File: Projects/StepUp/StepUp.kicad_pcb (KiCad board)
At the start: 2 copper layers, 53 parts, among them J1 Conn_01x02, J2 USB_B_Micro, U1 TMC2300-LA, U2 NCP1117-3.3_SOT223, U3 MIC2253, U4 W25Q128JVS, U5 RP2040, U6 COM-09032, U7 MCP73832T-2ACI_OT, U8 USBLC6-2SC6, Y1 ABM8-272-T3

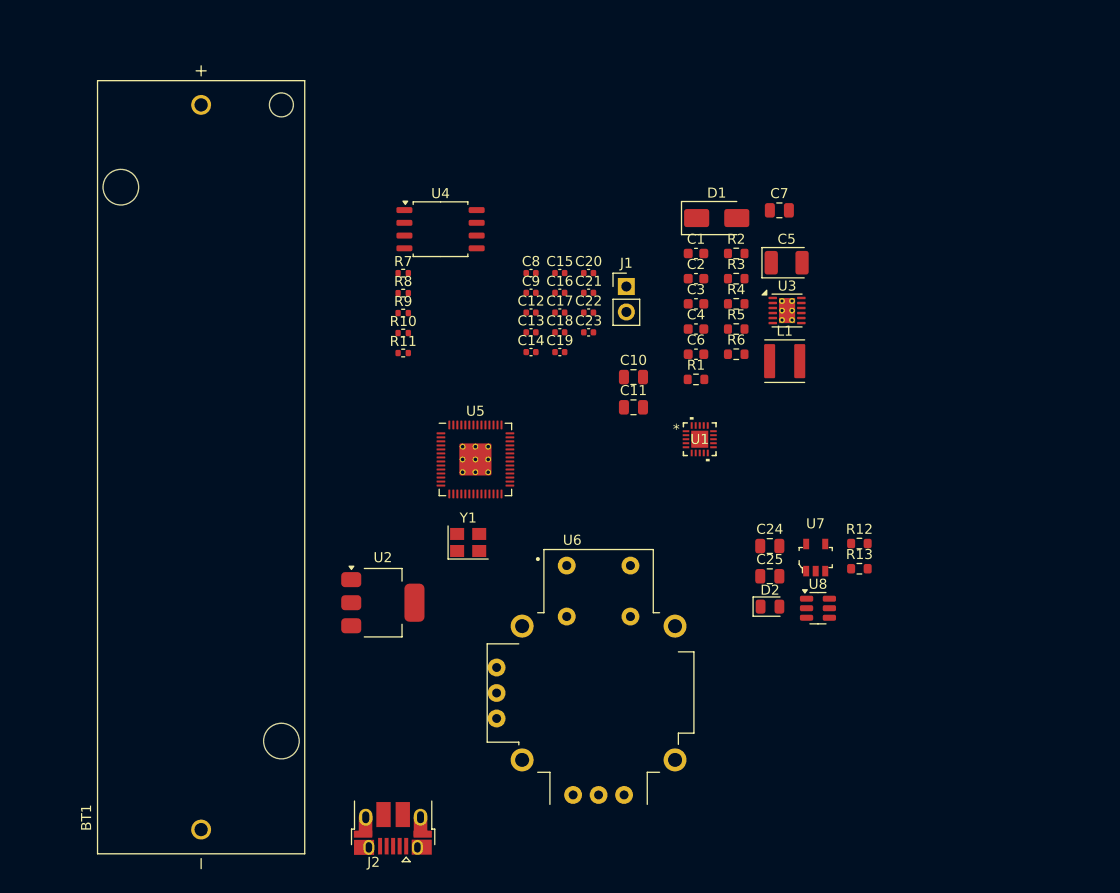
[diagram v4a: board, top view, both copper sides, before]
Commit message: feat(power): Input stage updates
USB vs Vbat source selection using PMOS gate logic.
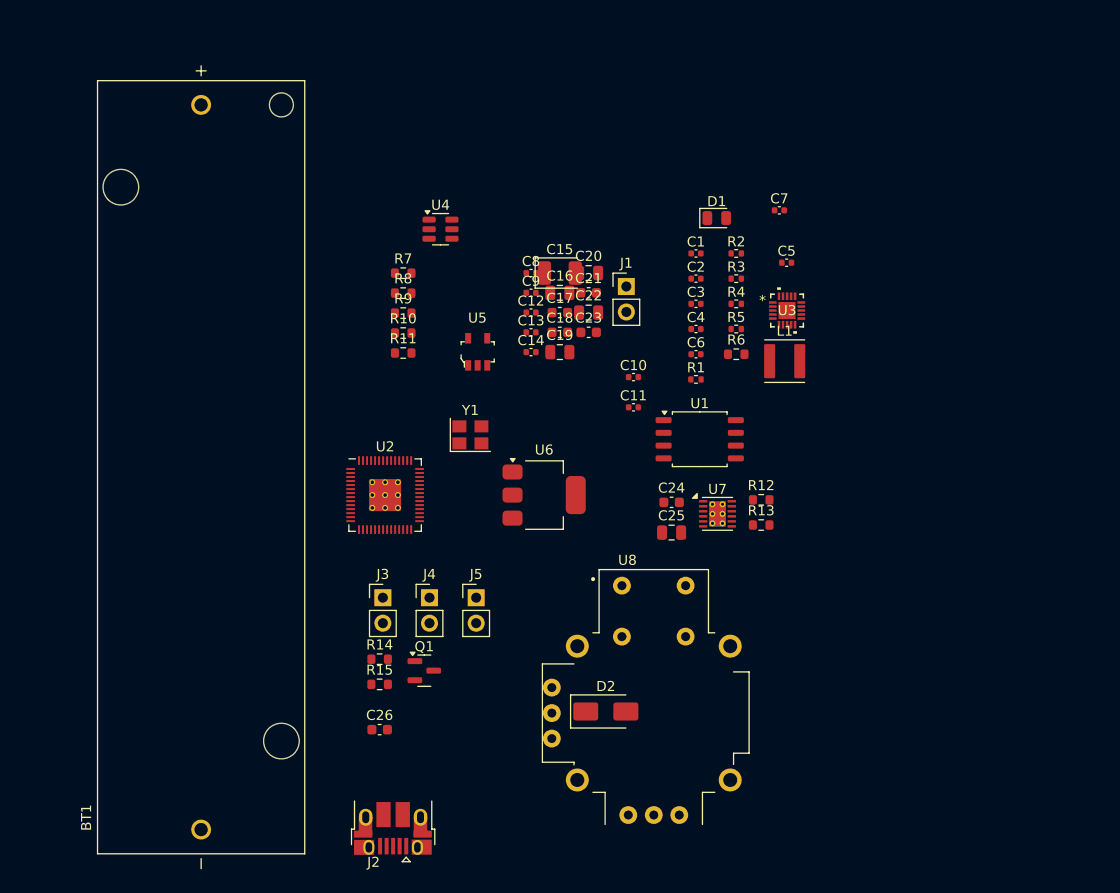
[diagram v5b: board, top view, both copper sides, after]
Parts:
- added C26: 0.1uF, Capacitor_SMD:C_0603_1608Metric, F.Cu at (122.2, 131.2)
- added J3: Conn_01x02, Connector_PinHeader_2.54mm:PinHeader_1x02_P2.54mm_Vertical, F.Cu at (122.5, 118.0)
- added J4: Conn_01x02, Connector_PinHeader_2.54mm:PinHeader_1x02_P2.54mm_Vertical, F.Cu at (127.2, 118.0)
- added J5: Conn_01x02, Connector_PinHeader_2.54mm:PinHeader_1x02_P2.54mm_Vertical, F.Cu at (131.8, 118.0)
- added Q1: BSS83P, Package_TO_SOT_SMD:SOT-23, F.Cu at (126.6, 125.3)
- added R14: 100R, Resistor_SMD:R_0603_1608Metric, F.Cu at (122.2, 124.1)
- added R15: 100kR, Resistor_SMD:R_0603_1608Metric, F.Cu at (122.2, 126.6)
- C1: value 0.1uF -> 15p; footprint Capacitor_SMD:C_0603_1608Metric -> Capacitor_SMD:C_0402_1005Metric
- C10, C11: value 10u -> 100n; footprint Capacitor_SMD:C_0805_2012Metric -> Capacitor_SMD:C_0402_1005Metric
- C15: value 1u -> 100uF; footprint Capacitor_SMD:C_0402_1005Metric -> Capacitor_Tantalum_SMD:CP_EIA-3528-12_Kemet-T
- C16, C19: value 100n -> 4.7u; footprint Capacitor_SMD:C_0402_1005Metric -> Capacitor_SMD:C_0805_2012Metric
- C17: value 1u -> 2.2uF; footprint Capacitor_SMD:C_0402_1005Metric -> Capacitor_SMD:C_0603_1608Metric
- C18, C23: value 100n -> 0.01uF; footprint Capacitor_SMD:C_0402_1005Metric -> Capacitor_SMD:C_0603_1608Metric
- C2: value 0.01uF -> 15p; footprint Capacitor_SMD:C_0603_1608Metric -> Capacitor_SMD:C_0402_1005Metric
- C20, C22: value 100n -> 10u; footprint Capacitor_SMD:C_0402_1005Metric -> Capacitor_SMD:C_0805_2012Metric
- C21: value 100n -> 0.1uF; footprint Capacitor_SMD:C_0402_1005Metric -> Capacitor_SMD:C_0603_1608Metric
- C24: value 4.7u -> 100pF; footprint Capacitor_SMD:C_0805_2012Metric -> Capacitor_SMD:C_0603_1608Metric
- C25: value 4.7u -> 22uF
- C3: value 0.01uF -> 100n; footprint Capacitor_SMD:C_0603_1608Metric -> Capacitor_SMD:C_0402_1005Metric
- C4: value 2.2uF -> 100n; footprint Capacitor_SMD:C_0603_1608Metric -> Capacitor_SMD:C_0402_1005Metric
- C5: value 100uF -> 100n; footprint Capacitor_Tantalum_SMD:CP_EIA-3528-12_Kemet-T -> Capacitor_SMD:C_0402_1005Metric
- C6: value 100pF -> 1u; footprint Capacitor_SMD:C_0603_1608Metric -> Capacitor_SMD:C_0402_1005Metric
- C7: value 22uF -> 100n; footprint Capacitor_SMD:C_0805_2012Metric -> Capacitor_SMD:C_0402_1005Metric
- C8: value 15p -> 1u
- C9: value 15p -> 100n
- D1: value SK54A-LTP -> LED; footprint Diode_SMD:D_SMA -> LED_SMD:LED_0805_2012Metric
- D2: value LED -> SK54A-LTP; footprint LED_SMD:LED_0805_2012Metric -> Diode_SMD:D_SMA
- R1: value 620R -> 1k; footprint Resistor_SMD:R_0603_1608Metric -> Resistor_SMD:R_0402_1005Metric
- R10: value 27 -> 71.5kR; footprint Resistor_SMD:R_0402_1005Metric -> Resistor_SMD:R_0603_1608Metric
- R11: value 1k -> 10kR; footprint Resistor_SMD:R_0402_1005Metric -> Resistor_SMD:R_0603_1608Metric
- R12: value RProg -> 9.09kR
- R13: value Rled -> 10kR
- R2: value 10kR -> DNF; footprint Resistor_SMD:R_0603_1608Metric -> Resistor_SMD:R_0402_1005Metric
- R3: value 9.09kR -> 1k; footprint Resistor_SMD:R_0603_1608Metric -> Resistor_SMD:R_0402_1005Metric
- R4: value 71.5kR -> 27; footprint Resistor_SMD:R_0603_1608Metric -> Resistor_SMD:R_0402_1005Metric
- R5: value 10kR -> 27; footprint Resistor_SMD:R_0603_1608Metric -> Resistor_SMD:R_0402_1005Metric
- R6: value 100kR -> RProg
- R7: value 1k -> Rled; footprint Resistor_SMD:R_0402_1005Metric -> Resistor_SMD:R_0603_1608Metric
- R8: value DNF -> 100kR; footprint Resistor_SMD:R_0402_1005Metric -> Resistor_SMD:R_0603_1608Metric
- R9: value 27 -> 620R; footprint Resistor_SMD:R_0402_1005Metric -> Resistor_SMD:R_0603_1608Metric
- U1: value TMC2300-LA -> W25Q128JVS; footprint footprints:QFN20_3x3_TRI-L -> Package_SO:SOIC-8_5.23x5.23mm_P1.27mm
- U2: value NCP1117-3.3_SOT223 -> RP2040; footprint Package_TO_SOT_SMD:SOT-223-3_TabPin2 -> RP2040_minimal_r2:RP2040-QFN-56
- U3: value MIC2253 -> TMC2300-LA; footprint Package_DFN_QFN:DFN-12-1EP_3x3mm_P0.5mm_EP1.6x2.5mm_ThermalVias -> Ultra_librarian_footprints:QFN20_3x3_TRI
- U4: value W25Q128JVS -> USBLC6-2SC6; footprint Package_SO:SOIC-8_5.23x5.23mm_P1.27mm -> Package_TO_SOT_SMD:SOT-23-6
- U5: value RP2040 -> MCP73832T-2ACI_OT; footprint RP2040_minimal_r2:RP2040-QFN-56 -> digikey-footprints:SOT-753
- U6: value COM-09032 -> NCP1117-3.3_SOT223; footprint joystick_footprints:XDCR_COM-09032 -> Package_TO_SOT_SMD:SOT-223-3_TabPin2
- U7: value MCP73832T-2ACI_OT -> MIC2253; footprint digikey-footprints:SOT-753 -> Package_DFN_QFN:DFN-12-1EP_3x3mm_P0.5mm_EP1.6x2.5mm_ThermalVias
- U8: value USBLC6-2SC6 -> COM-09032; footprint Package_TO_SOT_SMD:SOT-23-6 -> joystick_footprints:XDCR_COM-09032
- moved U6 20.5 mm to (138.6, 107.8)
- moved D2 19.4 mm to (144.7, 129.3)
- moved U8 19.4 mm to (149.5, 129.5)
- moved U2 10.7 mm to (122.7, 107.8)
- moved U5 10.7 mm to (131.9, 93.5)
- moved Y1 10.7 mm to (131.2, 101.8)
- moved C24 10.7 mm to (151.3, 108.5)
- moved R12 10.7 mm to (160.2, 108.2)
- moved U7 10.7 mm to (155.8, 109.6)
- moved C25 10.7 mm to (151.3, 111.5)
- moved R13 10.7 mm to (160.2, 110.8)
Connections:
- C1 pad 1: Net-(U3-SS) -> /MCU/XIN
- C10 pad 1: VBUS -> +3V3
- C13 pad 1: +1V1 -> +3V3
- C14 pad 1: +1V1 -> +3V3
- C15 pad 1: +1V1 -> /Power/BOOST_VIN
- C16 pad 1: +3V3 -> GND
- C16 pad 2: GND -> VBUS
- C17 pad 1: +3V3 -> /Power/BOOST_VIN
- C18 pad 1: +3V3 -> /Power/BOOST_VIN
- C19 pad 1: +3V3 -> Net-(J4-Pin_2)
- C20 pad 1: +3V3 -> Net-(J3-Pin_2)
- C21 pad 1: +3V3 -> Net-(U7-SS)
- C23 pad 1: +3V3 -> Net-(C23-Pad1)
- C24 pad 1: GND -> /Power/BOOST_VOUT
- C24 pad 2: VBUS -> Net-(U7-FB)
- C25 pad 1: /Power/Vbat -> /Power/BOOST_VOUT
- C3 pad 1: /Power/BOOST_VIN -> +3V3
- C4 pad 1: /Power/BOOST_VIN -> +1V1
- C5 pad 1: /Power/BOOST_VIN -> +1V1
- C6 pad 1: /Power/BOOST_VOUT -> +1V1
- C6 pad 2: Net-(U3-FB) -> GND
- C7 pad 1: /Power/BOOST_VOUT -> +3V3
- C8 pad 1: /MCU/XIN -> +3V3
- C9 pad 1: Net-(C9-Pad1) -> +3V3
- D1 pad 1: /Power/BOOST_VOUT -> Net-(D1-K)
- D1 pad 2: Net-(D1-A) -> VBUS
- D2 pad 1: Net-(D2-K) -> /Power/BOOST_VOUT
- D2 pad 2: VBUS -> Net-(D2-A)
- J2 pad 1: VBUS -> Net-(J2-VBUS)
- L1 pad 2: Net-(D1-A) -> Net-(D2-A)
- R1 pad 1: Net-(U3-COMP) -> /MCU/QSPI_SS
- R1 pad 2: Net-(C2-Pad1) -> /MCU/~{USB_BOOT}
- R10 pad 1: /MCU/USB_D- -> Net-(U7-OVP)
- R10 pad 2: Net-(U5-USB_DM) -> /Power/BOOST_VOUT
- R11 pad 1: /MCU/XOUT -> GND
- R11 pad 2: Net-(C9-Pad1) -> Net-(U7-OVP)
- R12 pad 1: GND -> Net-(U7-FB)
- R12 pad 2: Net-(U7-PROG) -> /Power/BOOST_VOUT
- R13 pad 1: Net-(U7-STAT) -> GND
- R13 pad 2: Net-(D2-K) -> Net-(U7-FB)
- R2 pad 1: GND -> +3V3
- R2 pad 2: Net-(U3-FB) -> /MCU/QSPI_SS
- R3 pad 1: Net-(U3-FB) -> /MCU/XOUT
- R3 pad 2: /Power/BOOST_VOUT -> Net-(C2-Pad1)
- R4 pad 1: Net-(U3-OVP) -> /MCU/USB_D+
- R4 pad 2: /Power/BOOST_VOUT -> Net-(U2-USB_DP)
- R5 pad 1: GND -> /MCU/USB_D-
- R5 pad 2: Net-(U3-OVP) -> Net-(U2-USB_DM)
- R6 pad 2: /Power/BOOST_ENABLE -> Net-(U5-PROG)
- R7 pad 1: /MCU/QSPI_SS -> Net-(U5-STAT)
- R7 pad 2: /MCU/~{USB_BOOT} -> Net-(D1-K)
- R8 pad 1: +3V3 -> GND
- R8 pad 2: /MCU/QSPI_SS -> /Power/BOOST_ENABLE
- R9 pad 1: /MCU/USB_D+ -> Net-(U7-COMP)
- R9 pad 2: Net-(U5-USB_DP) -> Net-(C23-Pad1)
- U1 pad 1: unconnected-(U1-OA2-Pad1) -> /MCU/QSPI_SS
- U1 pad 2: unconnected-(U1-VCP-Pad2) -> /MCU/QSPI_SD1
- U1 pad 3: unconnected-(U1-DIR-Pad3) -> /MCU/QSPI_SD2
- U1 pad 4: unconnected-(U1-STEP-Pad4) -> GND
- U1 pad 5: unconnected-(U1-MS1_AD0-Pad5) -> /MCU/QSPI_SD0
- U1 pad 6: unconnected-(U1-MS2_AD1-Pad6) -> /MCU/QSPI_SCLK
- U1 pad 7: unconnected-(U1-EN-Pad7) -> /MCU/QSPI_SD3
- U1 pad 8: unconnected-(U1-STEPPER-Pad8) -> +3V3
- U2 pad 1: GND -> +3V3
- U2 pad 2: +3V3 -> /MCU/GPIO0
- U2 pad 3: VBUS -> /MCU/GPIO1
- U3 pad 10: /Power/BOOST_VIN -> unconnected-(U3-PDN_UART-Pad10)
- U3 pad 11: /Power/BOOST_ENABLE -> unconnected-(U3-VIO/NSTDBY-Pad11)
- U3 pad 12: Net-(U3-COMP) -> unconnected-(U3-DIAG-Pad12)
- U3 pad 13: GND -> unconnected-(U3-1.8VOUT-Pad13)
- U3 pad 2: Net-(U3-SS) -> unconnected-(U3-VCP-Pad2)
- U3 pad 3: Net-(U3-FB) -> unconnected-(U3-DIR-Pad3)
- U3 pad 4: GND -> unconnected-(U3-STEP-Pad4)
- U3 pad 5: GND -> unconnected-(U3-MS1_AD0-Pad5)
- U3 pad 6: GND -> unconnected-(U3-MS2_AD1-Pad6)
- U3 pad 7: Net-(D1-A) -> unconnected-(U3-EN-Pad7)
- U3 pad 8: Net-(D1-A) -> unconnected-(U3-STEPPER-Pad8)
- U3 pad 9: Net-(U3-OVP) -> unconnected-(U3-MODE-Pad9)
- U4 pad 1: /MCU/QSPI_SS -> /Power/USB_D+_IN
- U4 pad 2: /MCU/QSPI_SD1 -> GND
- U4 pad 3: /MCU/QSPI_SD2 -> /Power/USB_D-_IN
- U4 pad 4: GND -> /Power/USB_D-
- U4 pad 5: /MCU/QSPI_SD0 -> Net-(J2-VBUS)
- U4 pad 6: /MCU/QSPI_SCLK -> /Power/USB_D+
- U5 pad 1: +3V3 -> Net-(U5-STAT)
- U5 pad 2: /MCU/GPIO0 -> GND
- U5 pad 3: /MCU/GPIO1 -> Net-(J4-Pin_2)
- U5 pad 4: /MCU/GPIO2 -> VBUS
- U5 pad 5: /MCU/GPIO3 -> Net-(U5-PROG)
- U7 pad 1: Net-(U7-STAT) -> unconnected-(U7-NC-Pad1)
- U7 pad 2: GND -> Net-(U7-SS)
- U7 pad 3: /Power/Vbat -> Net-(U7-FB)
- U7 pad 4: VBUS -> GND
- U7 pad 5: Net-(U7-PROG) -> GND
- Y1 pad 3: Net-(C9-Pad1) -> Net-(C2-Pad1)

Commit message: feat(stepup): Many additions
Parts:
- removed J2: USB_B_Micro, Connector_USB:USB_Micro-B_Amphenol_10103594-0001LF_Horizontal
- removed J3: Conn_01x02, Connector_PinHeader_2.54mm:PinHeader_1x02_P2.54mm_Vertical
- added C27: 0.1uF, Capacitor_SMD:C_0603_1608Metric, F.Cu at (179.2, 86.7)
- added C30: 0.1uF, Capacitor_SMD:C_0603_1608Metric, F.Cu at (179.2, 89.2)
- added D3: PMEG2020EH, Diode_SMD:D_SOD-123F, F.Cu at (136.1, 139.5)
- added D4: CLX6F-FKC, LED_SMD:LED_RGB_PLCC-6, F.Cu at (184.9, 116.9)
- added D5: 1N4148W-TP, digikey-footprints:SOD-123, F.Cu at (191.8, 87.1)
- added H1: MountingHole, MountingHole:MountingHole_2.7mm_M2.5, F.Cu at (89.5, 65.5)
- added H2: MountingHole, MountingHole:MountingHole_2.7mm_M2.5, F.Cu at (88.5, 143.5)
- added H3: MountingHole, MountingHole:MountingHole_2.7mm_M2.5, F.Cu at (180.0, 66.5)
- added H4: MountingHole, MountingHole:MountingHole_2.7mm_M2.5, F.Cu at (181.0, 141.5)
- added J7: Conn_01x02, Connector_PinHeader_2.54mm:PinHeader_1x02_P2.54mm_Vertical, F.Cu at (177.5, 124.2)
- added J8: USB_C_Receptacle_USB2.0_16P, Connector_USB:USB_C_Receptacle_GCT_USB4105-xx-A_16P_TopMnt_Horizontal, F.Cu at (166.5, 141.0)
- added JP1: SolderJumper_2_Open, Jumper:SolderJumper-2_P1.3mm_Open_RoundedPad1.0x1.5mm, F.Cu at (183.3, 99.0)
- added Q2: BSS83P, Package_TO_SOT_SMD:SOT-23, F.Cu at (183.6, 95.0)
- added R16: 5.1kR, Resistor_SMD:R_0603_1608Metric, F.Cu at (166.2, 122.0)
- added R17: 5.1kR, Resistor_SMD:R_0603_1608Metric, F.Cu at (166.2, 124.5)
- added R18: 10kR, Resistor_SMD:R_0603_1608Metric, F.Cu at (179.2, 91.7)
- added R19: 100kR, Resistor_SMD:R_0603_1608Metric, F.Cu at (179.2, 94.2)
- added R20: 100kR, Resistor_SMD:R_0603_1608Metric, F.Cu at (179.2, 96.7)
- added R21: 100kR, Resistor_SMD:R_0603_1608Metric, F.Cu at (179.2, 99.2)
- added R22: 100kR, Resistor_SMD:R_0603_1608Metric, F.Cu at (179.2, 101.7)
- added SW1: SW_Push, Button_Switch_SMD:SW_Push_1P1T_NO_Vertical_Wuerth_434133025816, F.Cu at (170.0, 104.0)
- added SW2: SW_Push, Button_Switch_SMD:SW_Push_1P1T_NO_Vertical_Wuerth_434133025816, F.Cu at (169.9, 113.1)
- moved J1 36.7 mm to (183.5, 87.7)
- moved D2 14.5 mm to (130.5, 132.0)
- moved U6 2.44 mm to (136.8, 109.5)
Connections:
- net /Power/Vbat renamed Vbat
- C16 pad 2: VBUS -> V_USB
- D1 pad 2: VBUS -> V_USB
- J1 pad 1: /MCU/~{USB_BOOT} -> V_USB
- J1 pad 2: GND -> Net-(D3-A)
- J5 pad 1: VBUS -> V_USB
- R14 pad 1: VBUS -> V_USB
- U2 pad 34: /MCU/GPIO22 -> JOYSTSICK_BUTTON
- U2 pad 37: /MCU/GPIO25 -> VUSB_monitor
- U2 pad 38: /MCU/GPIO26_ADC0 -> JOYSTSICK_AXIS_V
- U2 pad 39: /MCU/GPIO27_ADC1 -> JOYSTSICK_AXIS_H
- U2 pad 40: /MCU/GPIO28_ADC2 -> Vbat_monitor
- U5 pad 4: VBUS -> V_USB
- U8 pad B1A: /User Input/JOYSTICK_BUTTON -> JOYSTSICK_BUTTON
- U8 pad H2: /User Input/JOYSTICK_AXIS_H -> JOYSTSICK_AXIS_H
- U8 pad V2: /User Input/JOYSTICK_AXIS_V -> JOYSTSICK_AXIS_V
